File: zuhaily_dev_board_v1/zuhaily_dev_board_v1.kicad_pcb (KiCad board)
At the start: 2 copper layers, 53 parts, among them J1 USB_B_Micro, J2 SD_Card, J3 DC_JACK, Q1 FS8205A, SW1 SW_DPDT_x2, SW2 SW_SPST, U1 74LVC245, U10 DW-01, U2 LM1117-5.0, U3 CH340G, U4 LM1117-3.3, U5 ATmega328-PU, U6 ESP-01v090, U7 TP4056, U8 LMV358, Y1 Crystal_12MHz, Y2 Crystal_16MHz

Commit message: generated pcb
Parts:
- removed Q_FDN340P1: MOSFET_P_CH, Package_TO_SOT_SMD:SOT-323_SC-70
- removed R9: 0.4, Resistor_THT:R_Axial_DIN0414_L11.9mm_D4.5mm_P15.24mm_Horizontal
- removed U6: ESP-01v090, Connector_PinHeader_2.54mm:PinHeader_2x04_P2.54mm_Vertical
- added J4: Conn_01x32_Female, Module:Arduino_UNO_R3, B.Cu at (82.5, 109.2)
- added Q2: FDN340P, Package_TO_SOT_SMD:SOT-323_SC-70, F.Cu at (81.3, 94.0)
- added SW3: SW_DIP_x04, Button_Switch_THT:SW_DIP_SPSTx04_Slide_9.78x12.34mm_W7.62mm_P2.54mm, F.Cu at (125.7, 61.0)
- added SW4: SW_DIP_x04, Button_Switch_THT:SW_DIP_SPSTx04_Slide_9.78x12.34mm_W7.62mm_P2.54mm, F.Cu at (125.7, 88.9)
- added SW5: SW_DIP_x04, Button_Switch_THT:SW_DIP_SPSTx04_Slide_9.78x12.34mm_W7.62mm_P2.54mm, F.Cu at (125.7, 102.9)
- added U_ESP1: ESP-01v090, Connector_PinHeader_2.54mm:PinHeader_2x04_P2.54mm_Vertical, F.Cu at (138.4, 87.6)
- BT1: footprint Battery:BatteryHolder_MPD_BH-18650-PC2 -> Battery:BatteryHolder_Keystone_1042_1x18650
- C10: value 0.1u -> 0.1uF
- C3: footprint Capacitor_SMD:CP_Elec_4x3.9 -> Capacitor_THT:CP_Radial_D5.0mm_P2.50mm
- C7: value C -> 0.1uF
- D2: value DIODE -> D
- D3, Q1, R12, R13, R14, R7, R8, U10, U7: moved to B.Cu
- J2: value SD_Card -> Micro_SD_Card; footprint Connector_Card:microSD_HC_Hirose_DM3D-SF -> sd_card_pretty:Conn_uSDcard; moved to B.Cu
- R1: footprint Package_TO_SOT_SMD:SuperSOT-3 -> Resistor_THT:R_Axial_DIN0207_L6.3mm_D2.5mm_P7.62mm_Horizontal
- R10, R11: footprint Resistor_THT:R_Axial_DIN0204_L3.6mm_D1.6mm_P5.08mm_Horizontal -> Resistor_THT:R_Axial_DIN0207_L6.3mm_D2.5mm_P7.62mm_Horizontal
- U1: footprint Package_DIP:DIP-20_W7.62mm_Socket_LongPads -> Package_SO:SOIC-20W_7.5x12.8mm_P1.27mm; moved to B.Cu
- U2, U4: footprint Package_TO_SOT_SMD:SOT-89-3 -> Package_TO_SOT_SMD:SOT-223
- U3: footprint Package_SO:SSOP-20_5.3x7.2mm_P0.65mm -> Package_SO:SOP-16_4.4x10.4mm_P1.27mm
- U5: footprint Module:Arduino_UNO_R3 -> Package_DIP:DIP-28_W7.62mm_Socket_LongPads
- moved C5 177.4 mm to (61.0, 95.2), turned to 180 degrees
- moved C6 175.2 mm to (68.6, 95.2), turned to 180 degrees
- moved D2 162.4 mm to (58.4, 82.5), turned to 180 degrees
- moved R11 158.1 mm to (63.5, 86.4), turned to 180 degrees
- moved R3 154.6 mm to (72.4, 109.2), turned to 180 degrees
- moved R7 150.4 mm to (94.0, 125.7), turned to 180 degrees
- moved D3 148.6 mm to (66.0, 118.1), turned to 270 degrees
- moved R10 146.2 mm to (55.9, 90.2)
- moved R1 145.2 mm to (78.7, 67.3), turned to 180 degrees
- moved C4 144.8 mm to (68.6, 102.9), turned to 180 degrees
- moved C9 144.5 mm to (94.0, 80.0), turned to 180 degrees
- moved U3 133.5 mm to (76.2, 76.2)
- moved C1 133.1 mm to (80.0, 88.9), turned to 90 degrees
- moved Y1 131.9 mm to (73.7, 86.4), turned to 180 degrees
- moved C2 128.8 mm to (69.8, 80.0), turned to 90 degrees
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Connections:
- C3 pad 1: /5V_REGULATED -> /5V_FILTERED
- C4 pad 1: /5V_REGULATED -> /5V_FILTERED
- C5 pad 1: /5V_REGULATED -> /5V_FILTERED
- C6 pad 1: /5V_REGULATED -> /5V_FILTERED
- D1 pad 2: /5V_REGULATED -> /5V_FILTERED
- D2 pad 1: Net-(D2-Pad1) -> /5V_REGULATOR_IN
- D2 pad 2: /5V_REGULATOR_IN -> Net-(D2-Pad2)
- D3 pad 1: (no net) -> /5V_FILTERED
- D3 pad 2: (no net) -> /BATT_OUT_POSITIVE
- J2 pad 1: /LEVEL_SHIFT_SD_CS -> Net-(J2-Pad1)
- J2 pad 2: /LEVEL_SHIFT_SD_MOSI -> /LEVEL_SHIFT_SD_CS
- J2 pad 3: GND -> /LEVEL_SHIFT_SD_MOSI
- J2 pad 7: /ARDUINO_SD_MISO -> Net-(J2-Pad7)
- J2 pad 9: Net-(J2-Pad9) -> GND
- J3 pad 2: Net-(D2-Pad1) -> Net-(D2-Pad2)
- R4 pad 1: /5V_REGULATED -> /5V_FILTERED
- R5 pad 2: /5V_REGULATED -> /5V_FILTERED
- R6 pad 1: /5V_REGULATED -> /5V_FILTERED
- U1 pad 5: /ARDUINO_LEVEL_SHIFT_SCK -> Net-(SW3-Pad8)
- U1 pad 6: /ARDUINO_LEVEL_SHIFT_CS -> Net-(SW3-Pad7)
- U1 pad 7: /ARDUINO_LEVEL_SHIFT_MOSI -> Net-(SW3-Pad6)
- U2 pad 2: /5V_REGULATED -> /5V_FILTERED
- U3 pad 16: /5V_REGULATED -> /5V_FILTERED
- U4 pad 3: /5V_REGULATED -> /5V_FILTERED
- U5 pad 11: Net-(U5-Pad11) -> /PD_5
- U5 pad 12: Net-(U5-Pad12) -> /PD_6
- U5 pad 13: Net-(U5-Pad13) -> /PD_7
- U5 pad 14: Net-(U5-Pad14) -> /PB_0
- U5 pad 15: Net-(U5-Pad15) -> /PB_1
- U5 pad 2: Net-(U5-Pad2) -> /ARDUINO_RX
- U5 pad 20: /5V_REGULATED -> /5V_FILTERED
- U5 pad 21: /5V_REGULATED -> /5V_FILTERED
- U5 pad 23: Net-(U5-Pad23) -> /PC_0
- U5 pad 24: Net-(U5-Pad24) -> /PC_1
- U5 pad 25: Net-(U5-Pad25) -> /PC_2
- U5 pad 26: Net-(U5-Pad26) -> /PC_3
- U5 pad 27: Net-(U5-Pad27) -> /PC_4
- U5 pad 28: Net-(U5-Pad28) -> /PC_5
- U5 pad 3: Net-(U5-Pad3) -> /ARDUINO_TX
- U5 pad 4: Net-(U5-Pad4) -> /PD_2
- U5 pad 5: Net-(U5-Pad5) -> /PD_3
- U5 pad 6: Net-(U5-Pad6) -> /PD_4
- U5 pad 7: /5V_REGULATED -> /5V_FILTERED
- U8 pad 4: Net-(U8-Pad4) -> GND
- U8 pad 8: Net-(U8-Pad8) -> /5V_FILTERED

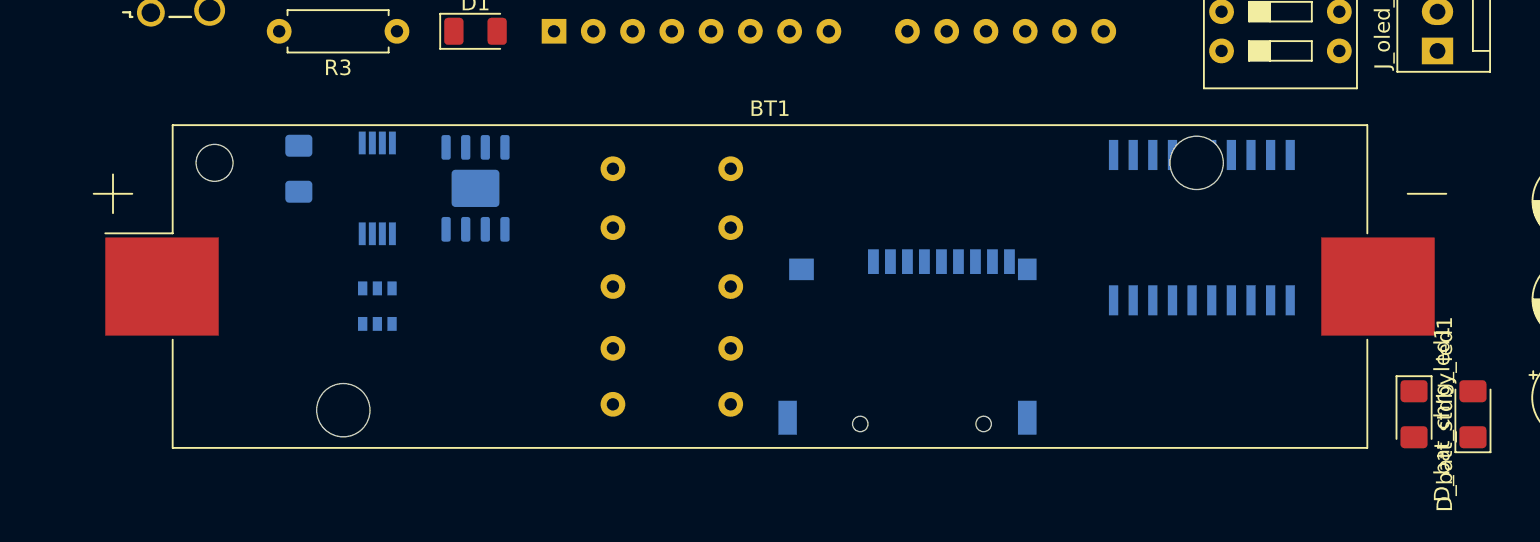
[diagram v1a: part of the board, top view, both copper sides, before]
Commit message: changed battery holder
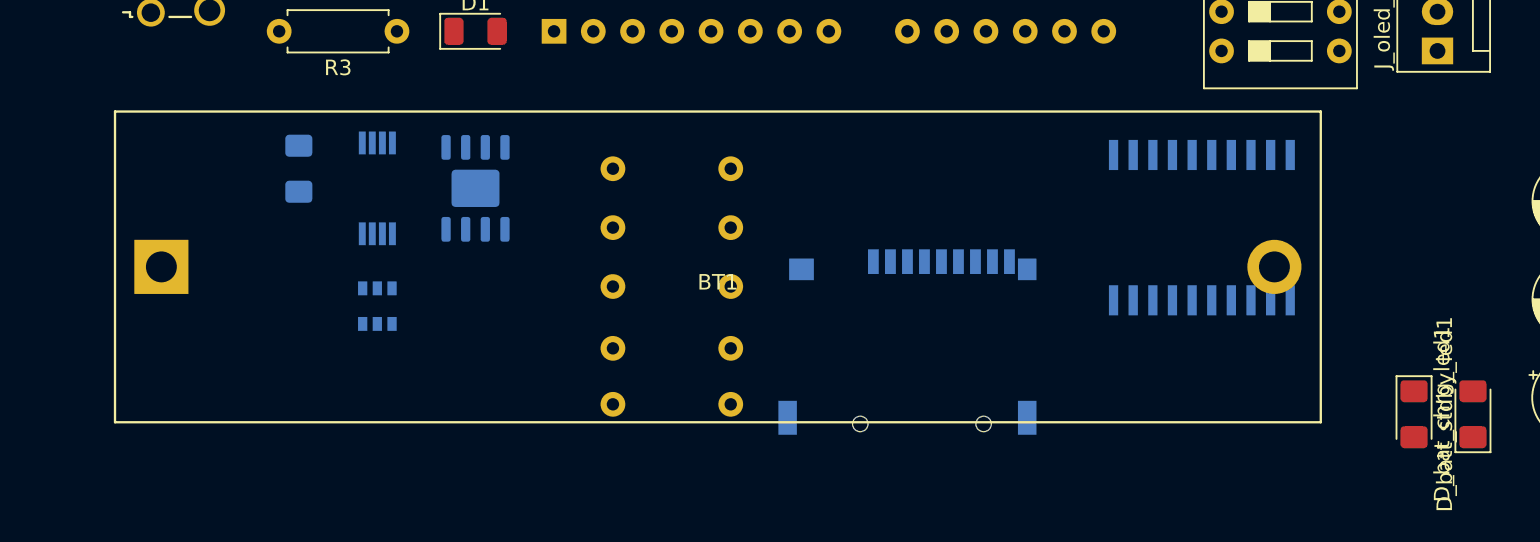
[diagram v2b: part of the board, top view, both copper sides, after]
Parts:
- BT1: footprint Battery:BatteryHolder_Keystone_1042_1x18650 -> Battery:BatteryHolder_MPD_BH-18650-PC2
- moved BT1 39.4 mm to (57.1, 124.5)
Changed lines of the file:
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@@
     (add_net "Net-(U_ESP1-Pad6)")
   )
-  (module Battery:BatteryHolder_Keystone_1042_1x18650 (layer F.Cu)
-    (at 96.52 125.73)
-    (descr "Battery holder for 18650 cylindrical cells http://www.keyelco.com/product.cfm/product_id/918")
-    (tags "18650 Keystone 1042 Li-ion")
-    (attr smd)
-    (fp_text reference BT1 (at 0 -11.5) (layer F.SilkS)
-      (effects (font (size 1 1) (thickness 0.15)))
-    )
-    (fp_text value Battery_Cell (at 0 11.3) (layer F.Fab)
-      (effects (font (size 1 1) (thickness 0.15)))
-    )
-    (fp_line (start -33.3675 -10.33) (end -38.53 -5.1675) (layer F.Fab) (width 0.1))
-    (fp_line (start -38.64 -3.44) (end -43 -3.44) (layer F.SilkS) (width 0.12))
-    (fp_line (start 43.5 3.68) (end 43.5 -3.68) (layer F.CrtYd) (width 0.05))
-    (fp_line (start 39.03 10.83) (end 39.03 3.68) (layer F.CrtYd) (width 0.05))
-    (fp_text user %R (at 0 0) (layer F.Fab)
-      (effects (font (size 1 1) (thickness 0.15)))
-    )
-    (fp_line (start -38.64 10.44) (end -38.64 3.44) (layer F.SilkS) (width 0.12))
-    (fp_line (start 38.64 10.44) (end -38.64 10.44) (layer F.SilkS) (width 0.12))
-    (fp_line (start 38.64 3.44) (end 38.64 10.44) (layer F.SilkS) (width 0.12))
-    (fp_line (start -38.64 -10.44) (end -38.64 -3.44) (layer F.SilkS) (width 0.12))
-    (fp_line (start 38.64 -10.44) (end -38.64 -10.44) (layer F.SilkS) (width 0.12))
-    (fp_line (start 38.64 -3.44) (end 38.64 -10.42) (layer F.SilkS) (width 0.12))
-    (fp_line (start -38.53 10.33) (end 38.53 10.33) (layer F.Fab) (width 0.1))
-    (fp_line (start -38.53 -5.1675) (end -38.53 10.33) (layer F.Fab) (width 0.1))
-    (fp_line (start 43.75 -6) (end 41.25 -6) (layer F.SilkS) (width 0.12))
-    (fp_line (start -33.3675 -10.33) (end 38.53 -10.33) (layer F.Fab) (width 0.1))
-    (fp_line (start 38.53 -10.33) (end 38.53 10.33) (layer F.Fab) (width 0.1))
-    (fp_line (start -39.03 10.83) (end 39.03 10.83) (layer F.CrtYd) (width 0.05))
-    (fp_line (start -39.03 -10.83) (end 39.03 -10.83) (layer F.CrtYd) (width 0.05))
-    (fp_line (start 39.03 -10.83) (end 39.03 -3.68) (layer F.CrtYd) (width 0.05))
-    (fp_line (start -39.03 10.83) (end -39.03 3.68) (layer F.CrtYd) (width 0.05))
-    (fp_line (start -39.03 -10.83) (end -39.03 -3.68) (layer F.CrtYd) (width 0.05))
-    (fp_line (start 39.03 3.68) (end 43.5 3.68) (layer F.CrtYd) (width 0.05))
-    (fp_line (start 43.5 -3.68) (end 39.03 -3.68) (layer F.CrtYd) (width 0.05))
-    (fp_line (start -43.5 -3.68) (end -39.03 -3.68) (layer F.CrtYd) (width 0.05))
-    (fp_line (start -43.5 3.68) (end -43.5 -3.68) (layer F.CrtYd) (width 0.05))
-    (fp_line (start -39.03 3.68) (end -43.5 3.68) (layer F.CrtYd) (width 0.05))
-    (fp_line (start -43.75 -6) (end -41.25 -6) (layer F.SilkS) (width 0.12))
-    (fp_line (start -42.5 -4.75) (end -42.5 -7.25) (layer F.SilkS) (width 0.12))
-    (pad 1 smd rect (at -39.33 0) (size 7.34 6.35) (layers F.Cu F.Paste F.Mask)
-      (net 2 /BATT_OUT_POSITIVE))
-    (pad 2 smd rect (at 39.33 0) (size 7.34 6.35) (layers F.Cu F.Paste F.Mask)
-      (net 1 "Net-(BT1-Pad2)"))
-    (pad "" np_thru_hole circle (at 27.6 -8) (size 3.45 3.45) (drill 3.45) (layers *.Cu *.Mask))
-    (pad "" np_thru_hole circle (at -27.6 8) (size 3.45 3.45) (drill 3.45) (layers *.Cu *.Mask))
-    (pad "" np_thru_hole circle (at -35.93 -8) (size 2.39 2.39) (drill 2.39) (layers *.Cu *.Mask))
-    (model ${KISYS3DMOD}/Battery.3dshapes/BatteryHolder_Keystone_1042_1x18650.wrl
-      (at (xyz 0 0 0))
-      (scale (xyz 1 1 1))
-      (rotate (xyz 0 0 0))
-    )
-  )
   (module Capacitor_THT:C_Disc_D4.7mm_W2.5mm_P5.00mm (layer F.Cu)
     (at 80.01 88.9 90)
@@
       (at (xyz 0 0 0))
       (scale (xyz 1 1 1))
+      (rotate (xyz 0 0 0))
+    )
+  )
+  (module Battery:BatteryHolder_MPD_BH-18650-PC2 (layer F.Cu)
+    (at 57.15 124.46)
+    (descr "18650 Battery Holder (http://www.memoryprotectiondevices.com/datasheets/BK-18650-PC2-datasheet.pdf)")
+    (tags "18650 Battery Holder")
+    (fp_text reference BT1 (at 36 1) (layer F.SilkS)
+      (effects (font (size 1 1) (thickness 0.15)))
+    )
+    (fp_text value Battery_Cell (at 36 -0.8) (layer F.Fab)
+      (effects (font (size 1 1) (thickness 0.15)))
+    )
+    (fp_line (start -3 10.05) (end -3 -10.05) (layer F.SilkS) (width 0.15))
+    (fp_line (start 75 10.05) (end -3 10.05) (layer F.SilkS) (width 0.15))
+    (fp_line (start 75 -10.05) (end 75 10.05) (layer F.SilkS) (width 0.15))
+    (fp_line (start -3 -10.05) (end 75 -10.05) (layer F.SilkS) (width 0.15))
+    (fp_line (start -2.8 9.85) (end -2.8 -9.85) (layer F.Fab) (width 0.15))
+    (fp_line (start 74.8 9.85) (end -2.8 9.85) (layer F.Fab) (width 0.15))
+    (fp_line (start 74.8 -9.85) (end 74.8 9.85) (layer F.Fab) (width 0.15))
+    (fp_line (start -2.8 -9.85) (end 74.8 -9.85) (layer F.Fab) (width 0.15))
+    (fp_line (start -3.2 10.25) (end -3.2 -10.25) (layer F.CrtYd) (width 0.05))
+    (fp_line (start 75.2 10.25) (end -3.2 10.25) (layer F.CrtYd) (width 0.05))
+    (fp_line (start 75.2 -10.25) (end 75.2 10.25) (layer F.CrtYd) (width 0.05))
+    (fp_line (start -3.2 -10.25) (end 75.2 -10.25) (layer F.CrtYd) (width 0.05))
+    (fp_text user %R (at 36 -2.4) (layer F.Fab)
+      (effects (font (size 1 1) (thickness 0.15)))
+    )
+    (pad 2 thru_hole circle (at 72 0) (size 3.5 3.5) (drill 2) (layers *.Cu *.Mask)
+      (net 1 "Net-(BT1-Pad2)"))
+    (pad 1 thru_hole rect (at 0 0) (size 3.5 3.5) (drill 2) (layers *.Cu *.Mask)
+      (net 2 /BATT_OUT_POSITIVE))
+    (model ${KISYS3DMOD}/Battery.3dshapes/BatteryHolder_MPD_BH-18650-PC2.wrl
+      (at (xyz 0 0 0))
+      (scale (xyz 1 1 1))

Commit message: added images
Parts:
- moved C12 11.7 mm to (137.0, 116.4)
- moved C11 11.7 mm to (137.0, 122.8)
- moved C10 8.80 mm to (144.8, 124.5), turned to 180 degrees
- moved U1 6.84 mm to (118.1, 124.5), turned to 180 degrees
- moved R7 6.48 mm to (87.6, 124.5)
- moved R8 6.48 mm to (87.6, 128.5)
- moved R12 6.48 mm to (80.0, 120.7)
- moved R13 6.48 mm to (80.0, 116.8)
- moved R14 6.48 mm to (80.0, 132.1)
- moved D3 6.35 mm to (59.7, 118.1)
- moved Q1 6.35 mm to (64.8, 119.4)
- moved U10 6.35 mm to (64.8, 127.0)
- moved U7 6.35 mm to (71.1, 119.4)
- moved J2 5.08 mm to (100.3, 134.6)
- moved D_bat_chrg_led1 4.71 mm to (137.8, 129.3), turned to 180 degrees
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
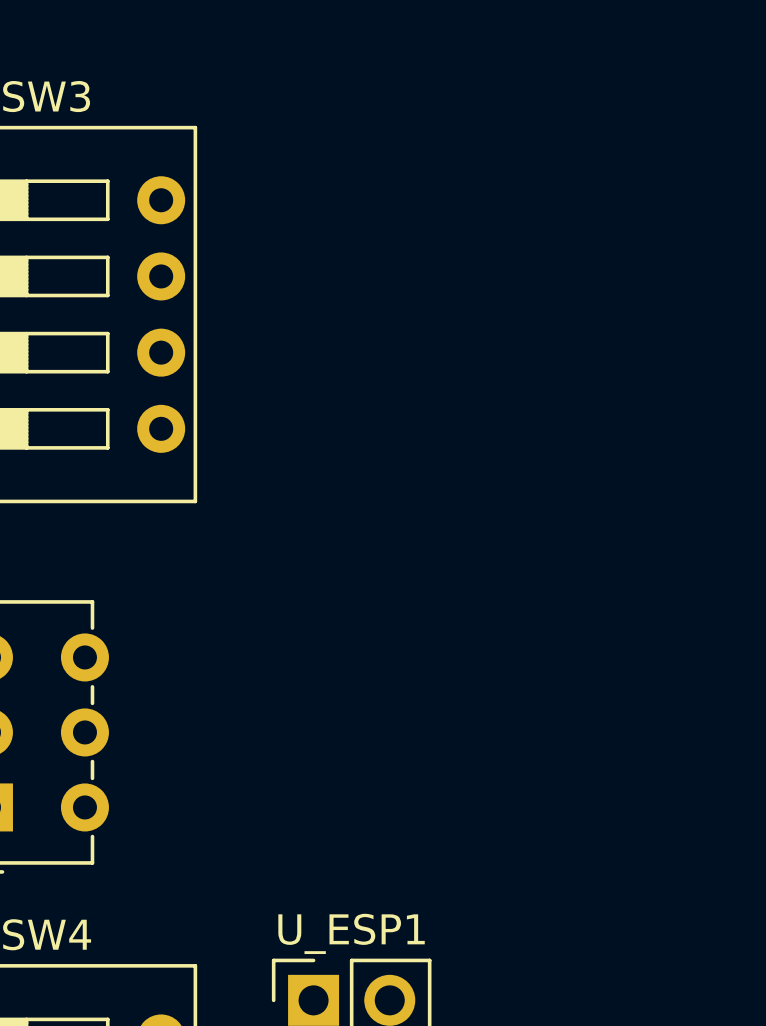
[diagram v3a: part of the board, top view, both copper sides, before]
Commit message: added rtc
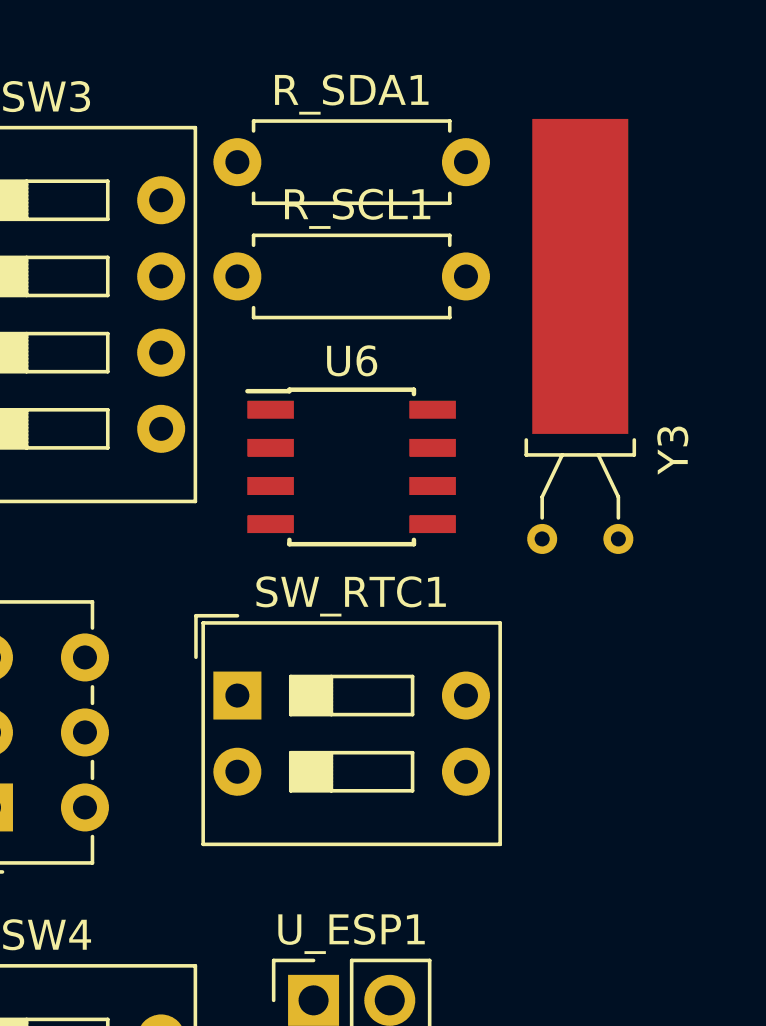
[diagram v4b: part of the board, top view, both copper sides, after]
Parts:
- added R_SCL1: 10k, Resistor_THT:R_Axial_DIN0207_L6.3mm_D2.5mm_P7.62mm_Horizontal, F.Cu at (135.9, 63.5)
- added R_SDA1: 10k, Resistor_THT:R_Axial_DIN0207_L6.3mm_D2.5mm_P7.62mm_Horizontal, F.Cu at (135.9, 59.7)
- added SW_RTC1: SW_DIP_x02, Button_Switch_THT:SW_DIP_SPSTx02_Slide_9.78x7.26mm_W7.62mm_P2.54mm, F.Cu at (135.9, 77.5)
- added U6: DS1307Z+, Package_SO:SOIC-8_3.9x4.9mm_P1.27mm, F.Cu at (139.7, 69.8)
- added Y3: Crystal_GND3, Crystal:Crystal_AT310_D3.0mm_L10.0mm_Horizontal_1EP_style1, F.Cu at (148.6, 72.2)

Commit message: working version without headers
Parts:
- moved J2 2.54 mm to (100.3, 132.1)
- moved J3 1.27 mm to (63.5, 73.7)
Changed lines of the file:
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@@
   (general
     (thickness 1.6)
-    (drawings 0)
+    (drawings 5)
     (tracks 0)
     (zones 0)
@@
   )
   (module sd_card_pretty:Conn_uSDcard (layer B.Cu)
-    (at 100.33 134.62 180)
+    (at 100.33 132.08 180)
     (fp_text reference J2 (at 0 -1) (layer B.Fab)
       (effects (font (size 0.6 0.6) (thickness 0.1)) (justify mirror))
@@
   )
   (module Connector_BarrelJack:BarrelJack_Horizontal (layer F.Cu)
-    (at 62.23 73.66)
+    (at 63.5 73.66)
     (descr "DC Barrel Jack")
     (tags "Power Jack")
@@
     )
   )
+  (dimension 78.74 (width 0.3) (layer F.SilkS)
+    (gr_text "78.740 mm" (at 92.71 148.15) (layer F.SilkS)
+      (effects (font (size 1.5 1.5) (thickness 0.3)))
+    )
+    (feature1 (pts (xy 132.08 140.97) (xy 132.08 146.636421)))
+    (feature2 (pts (xy 53.34 140.97) (xy 53.34 146.636421)))
+    (crossbar (pts (xy 53.34 146.05) (xy 132.08 146.05)))
+    (arrow1a (pts (xy 132.08 146.05) (xy 130.953496 146.636421)))
+    (arrow1b (pts (xy 132.08 146.05) (xy 130.953496 145.463579)))
+    (arrow2a (pts (xy 53.34 146.05) (xy 54.466504 146.636421)))
+    (arrow2b (pts (xy 53.34 146.05) (xy 54.466504 145.463579)))
+  )
+  (dimension 20.32 (width 0.3) (layer F.SilkS)
+    (gr_text "20.320 mm" (at 41.08 124.46 270) (layer F.SilkS)
+      (effects (font (size 1.5 1.5) (thickness 0.3)))
+    )
+    (feature1 (pts (xy 50.8 134.62) (xy 42.593579 134.62)))
+    (feature2 (pts (xy 50.8 114.3) (xy 42.593579 114.3)))
+    (crossbar (pts (xy 43.18 114.3) (xy 43.18 134.62)))
+    (arrow1a (pts (xy 43.18 134.62) (xy 42.593579 133.493496)))
+    (arrow1b (pts (xy 43.18 134.62) (xy 43.766421 133.493496)))
+    (arrow2a (pts (xy 43.18 114.3) (xy 42.593579 115.426504)))
+    (arrow2b (pts (xy 43.18 114.3) (xy 43.766421 115.426504)))
+  )
+  (dimension 53.475898 (width 0.3) (layer F.SilkS)
+    (gr_text "53.476 mm" (at 34.73 85.157949 270) (layer F.SilkS)
+      (effects (font (size 1.5 1.5) (thickness 0.3)))
+    )
+    (feature1 (pts (xy 44.45 111.895898) (xy 36.243579 111.895898)))
+    (feature2 (pts (xy 44.45 58.42) (xy 36.243579 58.42)))
+    (crossbar (pts (xy 36.83 58.42) (xy 36.83 111.895898)))
+    (arrow1a (pts (xy 36.83 111.895898) (xy 36.243579 110.769394)))
+    (arrow1b (pts (xy 36.83 111.895898) (xy 37.416421 110.769394)))
+    (arrow2a (pts (xy 36.83 58.42) (xy 36.243579 59.546504)))
+    (arrow2b (pts (xy 36.83 58.42) (xy 37.416421 59.546504)))
+  )
+  (dimension 67.32198 (width 0.3) (layer F.SilkS)
+    (gr_text "67.322 mm" (at 88.27099 46.16) (layer F.SilkS)
+      (effects (font (size 1.5 1.5) (thickness 0.3)))
+    )
+    (feature1 (pts (xy 121.93198 53.34) (xy 121.93198 47.673579)))
+    (feature2 (pts (xy 54.61 53.34) (xy 54.61 47.673579)))
+    (crossbar (pts (xy 54.61 48.26) (xy 121.93198 48.26)))
+    (arrow1a (pts (xy 121.93198 48.26) (xy 120.805476 48.846421)))
+    (arrow1b (pts (xy 121.93198 48.26) (xy 120.805476 47.673579)))
+    (arrow2a (pts (xy 54.61 48.26) (xy 55.736504 48.846421)))
+    (arrow2b (pts (xy 54.61 48.26) (xy 55.736504 47.673579)))
+  )
+  (dimension 96.595168 (width 0.3) (layer F.SilkS)
+    (gr_text "96.595 mm" (at 102.907584 158.31) (layer F.SilkS)
+      (effects (font (size 1.5 1.5) (thickness 0.3)))
+    )
+    (feature1 (pts (xy 151.205168 151.13) (xy 151.205168 156.796421)))
+    (feature2 (pts (xy 54.61 151.13) (xy 54.61 156.796421)))
+    (crossbar (pts (xy 54.61 156.21) (xy 151.205168 156.21)))
+    (arrow1a (pts (xy 151.205168 156.21) (xy 150.078664 156.796421)))
+    (arrow1b (pts (xy 151.205168 156.21) (xy 150.078664 155.623579)))
+    (arrow2a (pts (xy 54.61 156.21) (xy 55.736504 156.796421)))
+    (arrow2b (pts (xy 54.61 156.21) (xy 55.736504 155.623579)))
+  )
   (zone (net 0) (net_name "") (layers F&B.Cu) (hatch edge 0.508)
